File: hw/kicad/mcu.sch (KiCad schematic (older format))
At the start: 36 parts

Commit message: Started working on power supplies
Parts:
- removed C?: 100n, symbol C
- removed C?: 22u, symbol C
- removed C?: 10u, symbol C
- removed U?: AZ1117CR-3.3, TO_SOT_Packages_SMD:SOT89-3_Housing, symbol AZ1117CR-3.3
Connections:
- net I_SENS_A: now also U?.8 (PC0/ADC123_IN10); no longer U?.26 (PB0/ADC12_IN8)
- net I_SENS_B: now also U?.9 (PC1/ADC123_IN11); no longer U?.27 (PB1/ADC12_IN9)
- net I_SENS_C: now also U?.10 (PC2/ADC123_IN12)
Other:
- note removed: "DRV8301: SPI1 (AF5)"
- note removed: "ESR < 20R"
- moved on the sheet: C?, P?, R?

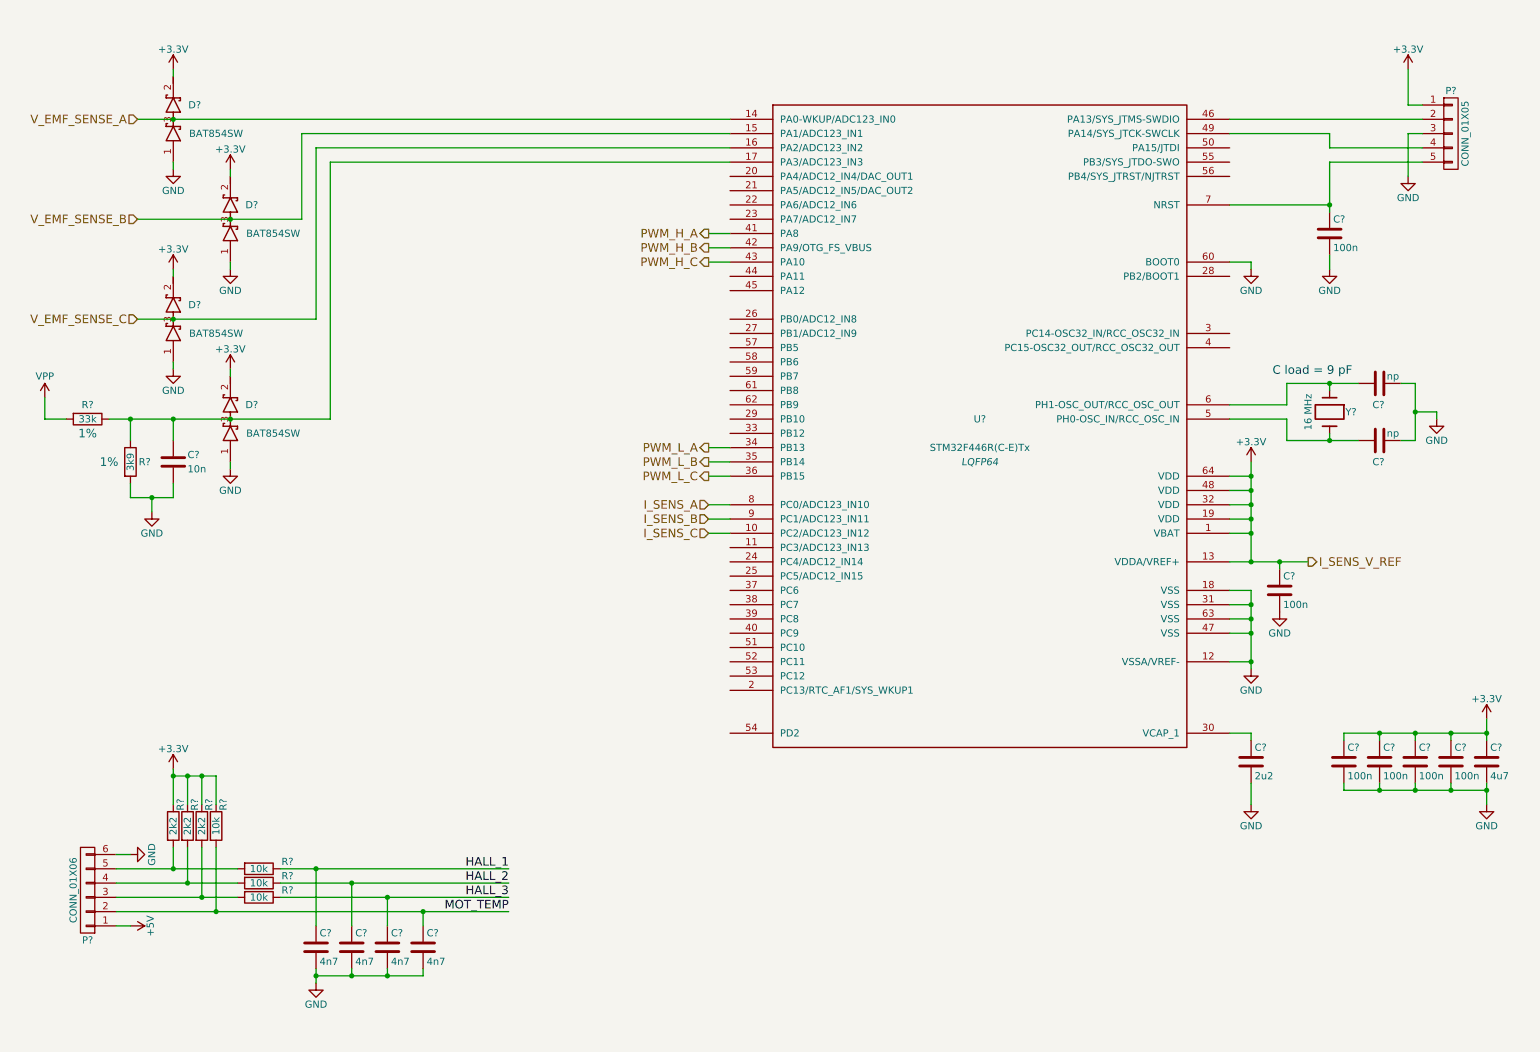
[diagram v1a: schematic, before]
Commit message: Gate power supply enabling and board temp sensor
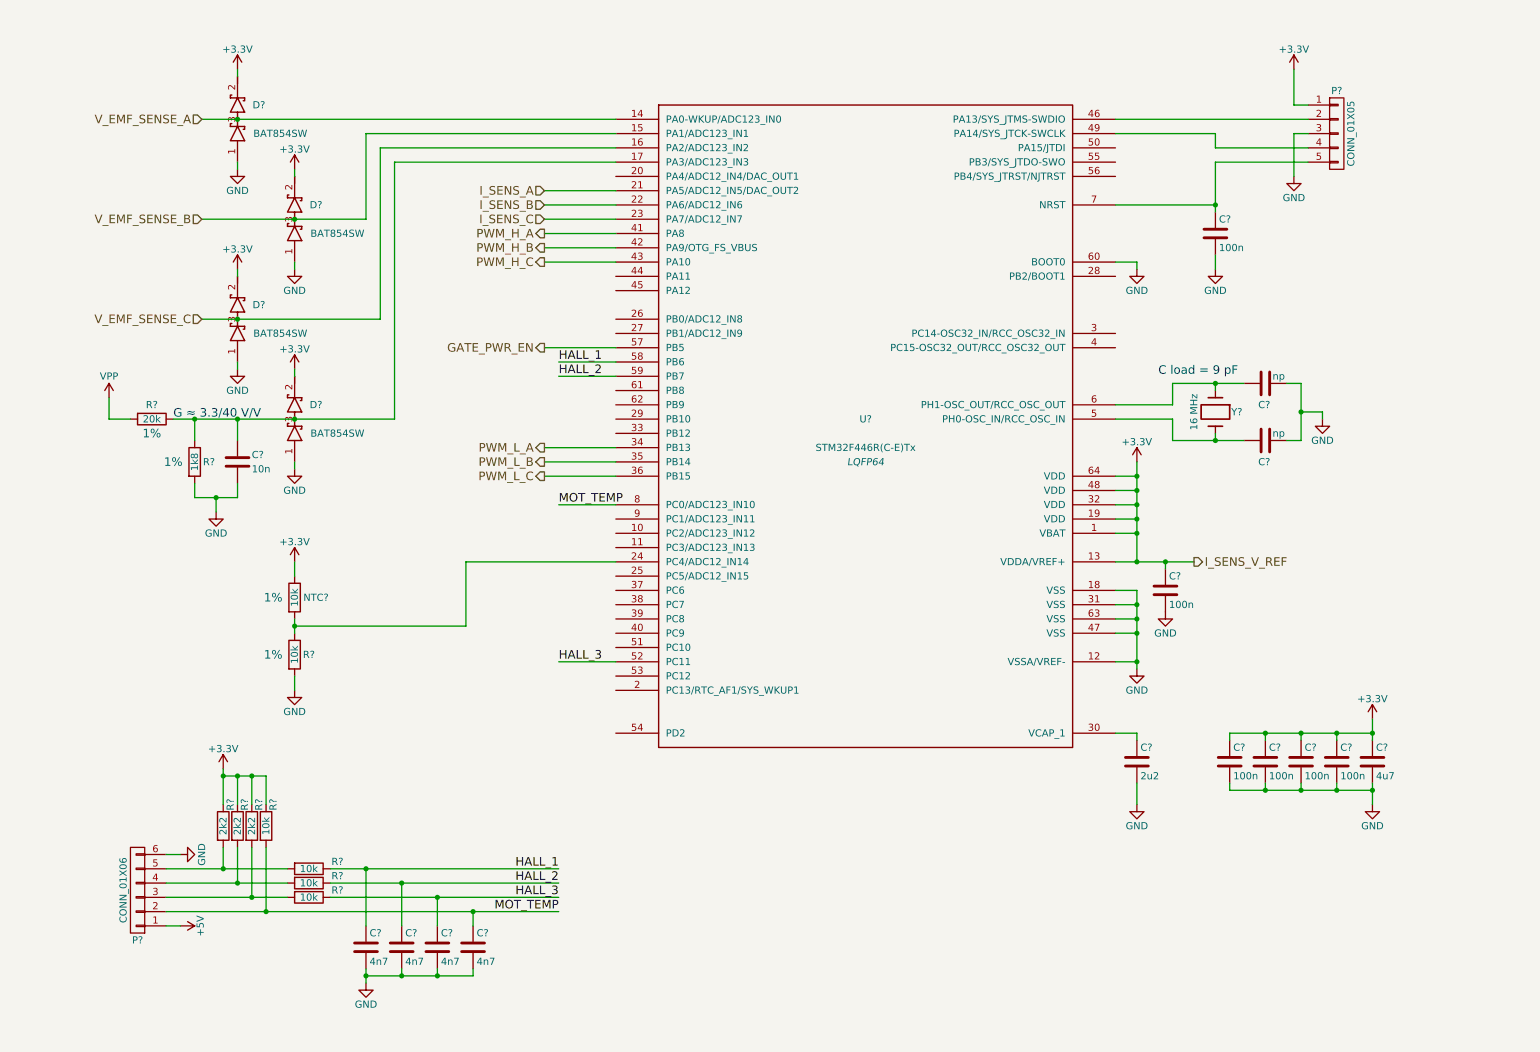
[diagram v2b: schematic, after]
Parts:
- added NTC?: 10k, Resistors_SMD:R_0603, symbol R
- added R?: 10k, symbol R
- R?: value 33k -> 20k
- R?: value 3k9 -> 1k8
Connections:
- net +3V3: now also NTC?.1
- net GND: now also R?.2
- net HALL_1: now also U?.58 (PB6)
- net HALL_2: now also U?.59 (PB7)
- net HALL_3: now also U?.52 (PC11)
- net I_SENS_A: now also U?.21 (PA5/ADC12_IN5/DAC_OUT2); no longer U?.8 (PC0/ADC123_IN10)
- net I_SENS_B: now also U?.22 (PA6/ADC12_IN6); no longer U?.9 (PC1/ADC123_IN11)
- net I_SENS_C: now also U?.23 (PA7/ADC12_IN7); no longer U?.10 (PC2/ADC123_IN12)
- net MOT_TEMP: now also U?.8 (PC0/ADC123_IN10)
- net at U?.24 (PC4/ADC12_IN14): now also NTC?.2, R?.1
- net GATE_PWR_EN: now reaches U?.57 (PB5)
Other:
- note added: "G ≈ 3.3/40 V/V"
- moved on the sheet: C?, D?, P?, R?, U?, Y?

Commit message: TVS across bat connection
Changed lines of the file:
@@
 LIBS:xilinx
 LIBS:Zilog
-LIBS:drv8301
 LIBS:wslp2726
 LIBS:test
@@
 	9000 6000 9000 5950
 Wire Wire Line
-	9000 6000 9250 6000
-Wire Wire Line
-	9250 6000 9500 6000
-Wire Wire Line
-	9500 6000 9750 6000
-Wire Wire Line
-	9750 6000 10000 6000
+	9000 6000 10000 6000
 Wire Wire Line
 	9000 5600 9000 5650
 Wire Wire Line
-	9000 5600 9250 5600
-Wire Wire Line
-	9250 5600 9500 5600
-Wire Wire Line
-	9500 5600 9750 5600
-Wire Wire Line
-	9750 5600 10000 5600
+	9000 5600 10000 5600
 Connection ~ 8350 4700
 Wire Wire Line
@@
 Connection ~ 8350 4900
 Wire Wire Line
-	8350 4600 8350 4700
-Wire Wire Line
-	8350 4700 8350 4800
-Wire Wire Line
-	8350 4800 8350 4900
-Wire Wire Line
-	8350 4900 8350 5100
-Wire Wire Line
-	8350 5100 8350 5150
+	8350 4600 8350 5150
 Wire Wire Line
 	8200 4600 8350 4600
@@
 	8350 4200 8200 4200
 Wire Wire Line
-	8350 3700 8350 3800
-Wire Wire Line
-	8350 3800 8350 3900
-Wire Wire Line
-	8350 3900 8350 4000
-Wire Wire Line
-	8350 4000 8350 4100
-Wire Wire Line
-	8350 4100 8350 4200
-Wire Wire Line
-	8350 4200 8350 4400
+	8350 3700 8350 4400
 Wire Wire Line
 	8200 3800 8350 3800
@@
 	9250 5950 9250 6000
 Wire Wire Line
-	10000 5950 10000 6000
-Wire Wire Line
-	10000 6000 10000 6100
-Wire Wire Line
-	10000 5500 10000 5600
-Wire Wire Line
-	10000 5600 10000 5650
+	10000 5950 10000 6100
+Wire Wire Line
+	10000 5500 10000 5650
 Wire Wire Line
 	8350 5600 8200 5600
@@
 	8350 4900 8200 4900
 Wire Wire Line
-	8200 4400 8350 4400
-Wire Wire Line
-	8350 4400 8550 4400
-Wire Wire Line
-	8550 4400 8750 4400
+	8200 4400 8750 4400
 Connection ~ 8350 4200
 Wire Wire Line
@@
 	9450 1400 9550 1400
 Wire Wire Line
-	8900 1600 8900 1900
-Wire Wire Line
-	8900 1900 8900 1950
+	8900 1600 8900 1950
 Connection ~ 8900 1900
 Wire Wire Line
@@
 	8600 3300 8600 3150
 Wire Wire Line
-	8600 3150 8900 3150
-Wire Wire Line
-	8900 3150 9100 3150
+	8600 3150 9100 3150
 Wire Wire Line
 	8900 3150 8900 3200
@@
 	8900 3500 8900 3550
 Wire Wire Line
-	8600 3550 8900 3550
-Wire Wire Line
-	8900 3550 9100 3550
+	8600 3550 9100 3550
 Wire Wire Line
 	8600 3550 8600 3400
@@
 	9400 3150 9500 3150
 Wire Wire Line
-	9500 3150 9500 3350
-Wire Wire Line
-	9500 3350 9500 3550
+	9500 3150 9500 3550
 Wire Wire Line
 	9500 3350 9650 3350
@@
 	2050 3050 2050 3000
 Wire Wire Line
-	1800 2700 2050 2700
-Wire Wire Line
-	2050 2700 3050 2700
+	1800 2700 3050 2700
 Wire Wire Line
 	2050 2400 2050 2350
@@
 Connection ~ 2450 2000
 Wire Wire Line
-	1800 1300 2050 1300
-Wire Wire Line
-	2050 1300 4700 1300
+	1800 1300 4700 1300
 Connection ~ 2050 1300
 Wire Wire Line
@@
 	4700 1400 2950 1400
 Wire Wire Line
-	2950 1400 2950 2000
-Wire Wire Line
-	2950 2000 2450 2000
-Wire Wire Line
-	2450 2000 1800 2000
+	2950 2000 2950 1400
+Wire Wire Line
+	1800 2000 2950 2000
 Wire Wire Line
 	3050 2700 3050 1500
@@
 	1550 6450 1650 6450
 Wire Wire Line
-	1550 6550 1950 6550
-Wire Wire Line
-	1950 6550 2400 6550
+	1550 6550 2400 6550
 Wire Wire Line
 	1950 6550 1950 6400
 Wire Wire Line
-	1550 6650 2050 6650
-Wire Wire Line
-	2050 6650 2400 6650
+	1550 6650 2400 6650
 Wire Wire Line
 	2050 6650 2050 6400
 Wire Wire Line
-	1550 6750 2150 6750
-Wire Wire Line
-	2150 6750 2400 6750
+	1550 6750 2400 6750
 Wire Wire Line
 	2150 6750 2150 6400
 Wire Wire Line
-	1550 6850 2250 6850
-Wire Wire Line
-	2250 6850 3700 6850
-Wire Wire Line
-	3700 6850 4300 6850
+	1550 6850 4300 6850
 Wire Wire Line
 	2250 6850 2250 6400
@@
 Connection ~ 2150 6750
 Wire Wire Line
-	2700 6550 2950 6550
-Wire Wire Line
-	2950 6550 4300 6550
+	2700 6550 4300 6550
 Wire Wire Line
 	2950 6550 2950 6950
 Wire Wire Line
-	2700 6650 3200 6650
-Wire Wire Line
-	3200 6650 4300 6650
+	2700 6650 4300 6650
 Wire Wire Line
 	3200 6650 3200 6950
 Wire Wire Line
-	2700 6750 3450 6750
-Wire Wire Line
-	3450 6750 4300 6750
+	2700 6750 4300 6750
 Wire Wire Line
 	3450 6750 3450 6950
 Wire Wire Line
-	2950 7250 2950 7300
-Wire Wire Line
-	2950 7300 2950 7350
-Wire Wire Line
-	2950 7300 3200 7300
-Wire Wire Line
-	3200 7300 3450 7300
-Wire Wire Line
-	3450 7300 3700 7300
+	2950 7250 2950 7350
+Wire Wire Line
+	2950 7300 3700 7300
 Wire Wire Line
 	3200 7300 3200 7250
@@
 $EndComp
 Wire Wire Line
-	1950 5850 1950 5900
-Wire Wire Line
-	1950 5900 1950 6100
-Wire Wire Line
-	1950 5900 2050 5900
-Wire Wire Line
-	2050 5900 2150 5900
-Wire Wire Line
-	2150 5900 2250 5900
+	1950 5850 1950 6100
+Wire Wire Line
+	1950 5900 2250 5900
 Wire Wire Line
 	2250 5900 2250 6100
@@
 	1900 3950 1900 4050
 Wire Wire Line
-	1750 3950 1900 3950
-Wire Wire Line
-	1900 3950 2050 3950
+	1750 3950 2050 3950
 Wire Wire Line
 	1750 3850 1750 3950
@@
 	2050 3400 2050 3550
 Wire Wire Line
-	1600 3400 1750 3400
-Wire Wire Line
-	1750 3400 2050 3400
-Wire Wire Line
-	2050 3400 2450 3400
-Wire Wire Line
-	2450 3400 3150 3400
+	1600 3400 3150 3400
 Connection ~ 2050 3400
 Wire Wire Line
@@
 	2450 5300 2450 5200
 Wire Wire Line
-	2450 4900 2450 4850
-Wire Wire Line
-	2450 4850 2450 4800
+	2450 4800 2450 4900
 Wire Wire Line
 	4700 4400 3650 4400

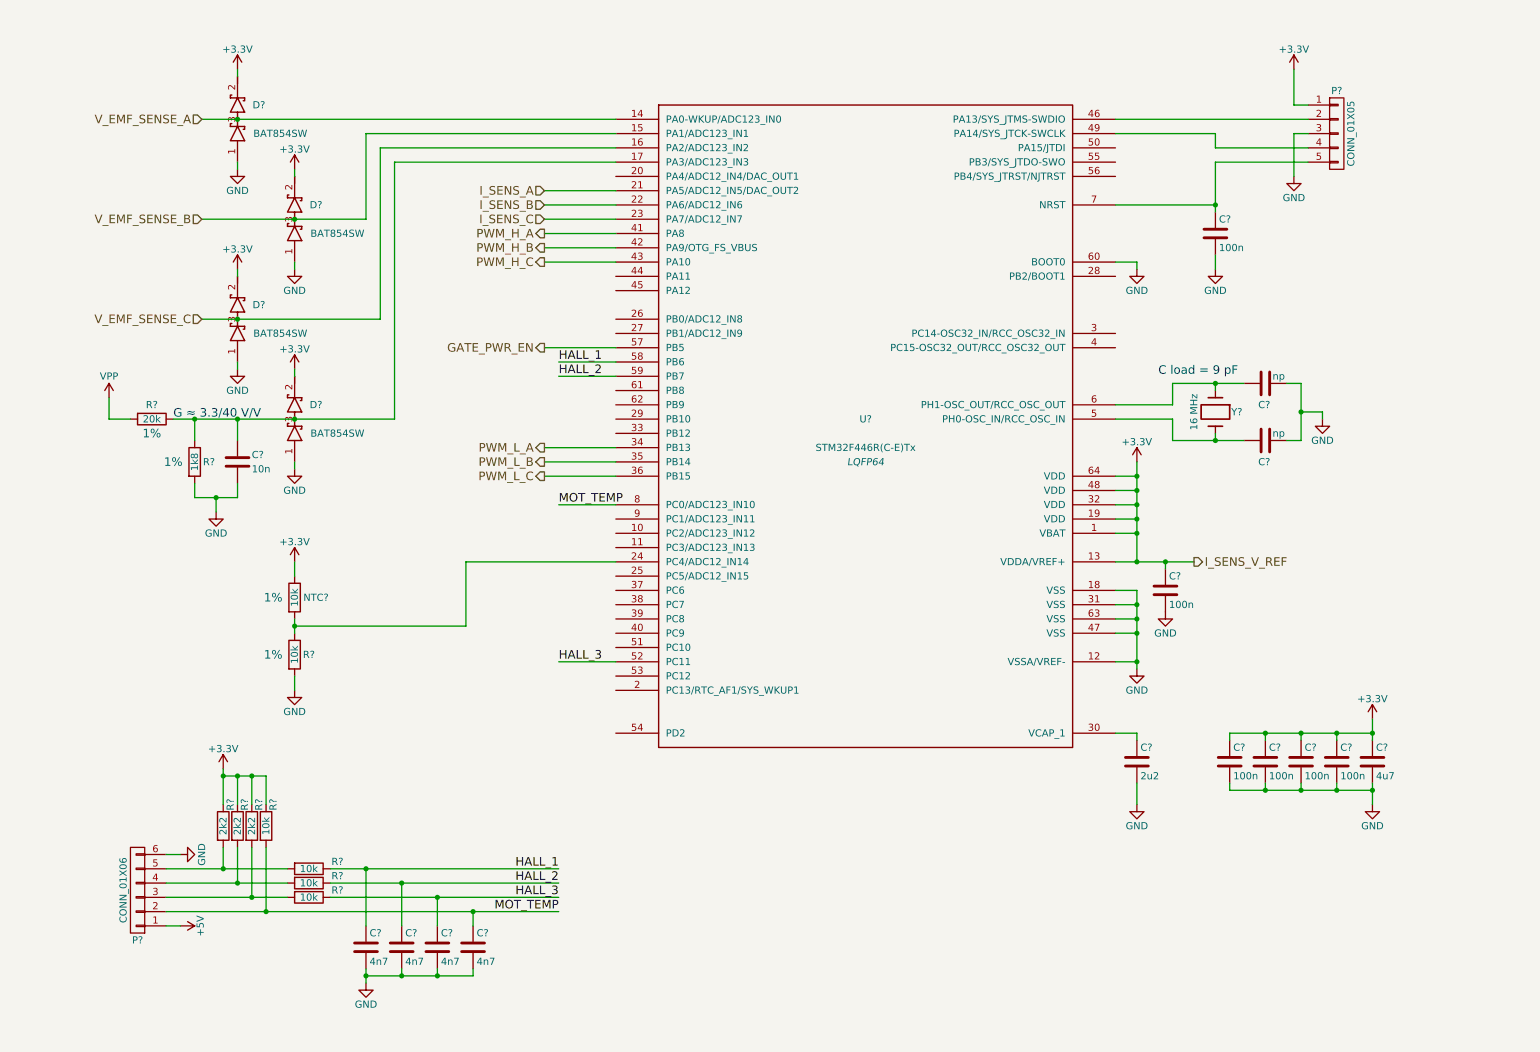
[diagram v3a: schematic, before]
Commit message: Bat pads and leds
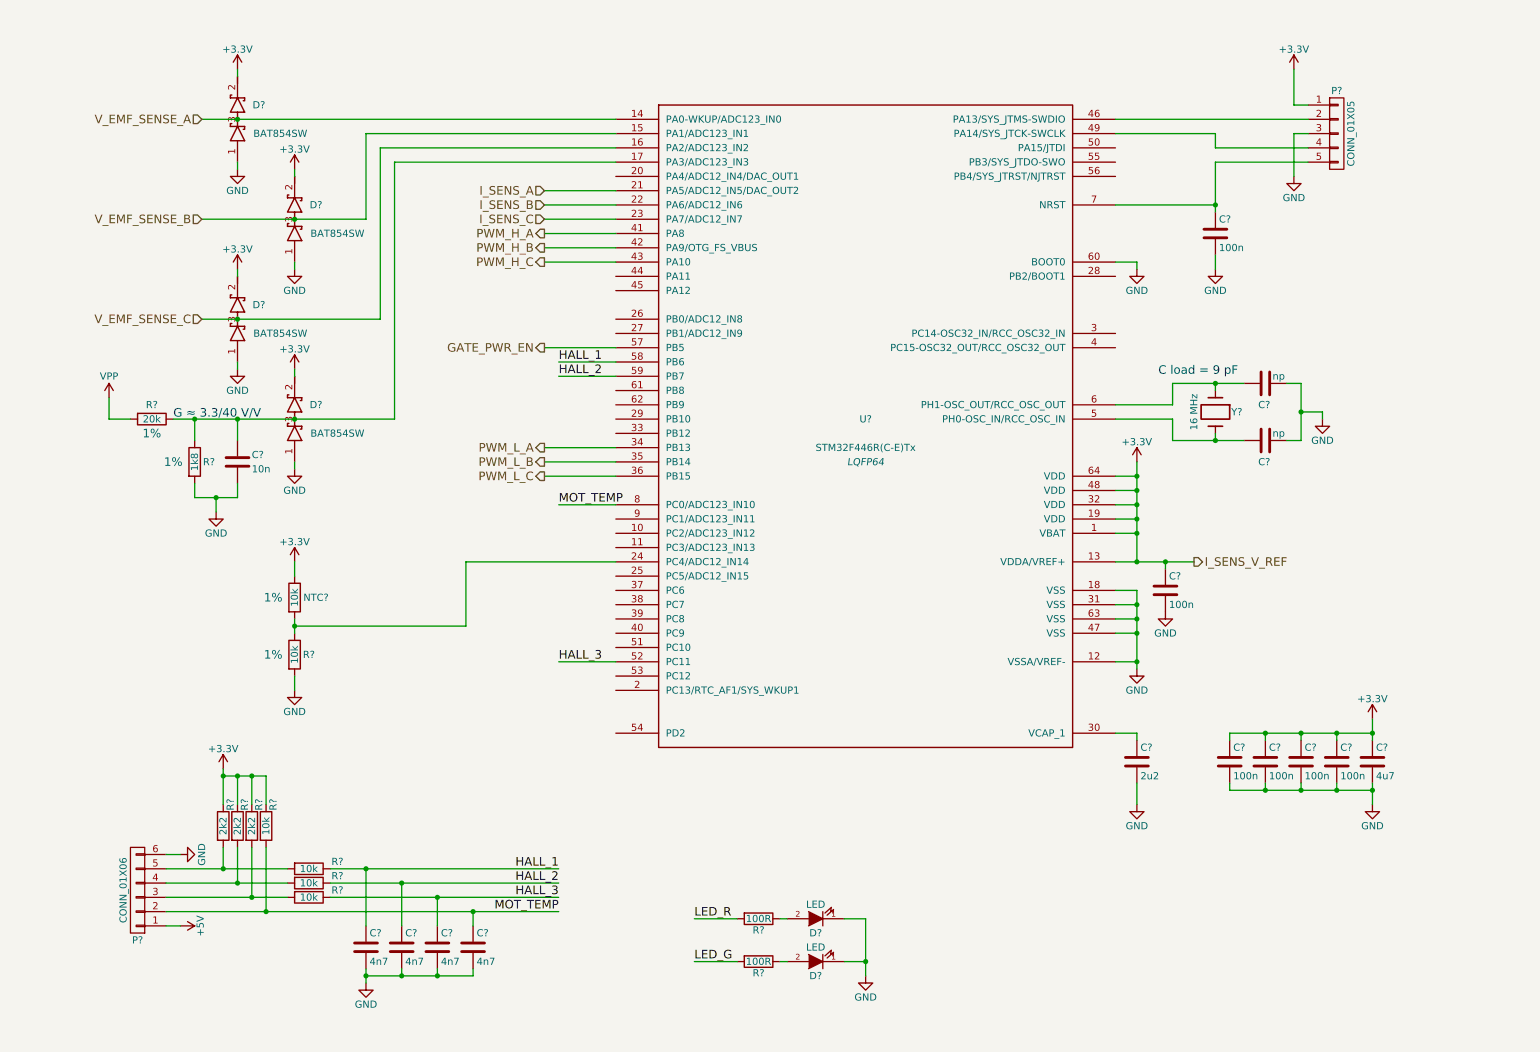
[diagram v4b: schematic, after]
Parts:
- added D? (x2): LED, symbol LED
- added R? (x2): 100R, symbol R
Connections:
- net GND: now also D?.1 (K), D?.1 (K)
- new net: D?.2 (A), R?.1 (x2)
- new net LED_G: R?.2
- new net LED_R: R?.2
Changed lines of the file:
@@
 	4700 1400 2950 1400
 Wire Wire Line
-	2950 2000 2950 1400
-Wire Wire Line
-	1800 2000 2950 2000
+	2950 1400 2950 2000
+Wire Wire Line
+	2950 2000 1800 2000
 Wire Wire Line
 	3050 2700 3050 1500
@@
 	3650 4850 3650 4400
 Connection ~ 2450 4850
+$Comp
+L LED D?
+U 1 1 58362F24
+P 6100 7200
+F 0 "D?" H 6100 7300 50  0000 C CNN
+F 1 "LED" H 6100 7100 50  0000 C CNN
+F 2 "" H 6100 7200 60  0000 C CNN
+F 3 "" H 6100 7200 60  0000 C CNN
+	1    6100 7200
+	-1   0    0    1
+$EndComp
+$Comp
+L LED D?
+U 1 1 583633B5
+P 6100 6900
+F 0 "D?" H 6100 7000 50  0000 C CNN
+F 1 "LED" H 6100 6800 50  0000 C CNN
+F 2 "" H 6100 6900 60  0000 C CNN
+F 3 "" H 6100 6900 60  0000 C CNN
+	1    6100 6900
+	-1   0    0    1
+$EndComp
+Wire Wire Line
+	6300 6900 6450 6900
+Wire Wire Line
+	6450 6900 6450 7300
+Wire Wire Line
+	6300 7200 6450 7200
+Connection ~ 6450 7200
+$Comp
+L GND #PWR?
+U 1 1 58363604
+P 6450 7300
+F 0 "#PWR?" H 6450 7050 50  0001 C CNN
+F 1 "GND" H 6450 7150 50  0000 C CNN
+F 2 "" H 6450 7300 60  0000 C CNN
+F 3 "" H 6450 7300 60  0000 C CNN
+	1    6450 7300
+	1    0    0    -1
+$EndComp
+$Comp
+L R R?
+U 1 1 58363C15
+P 5700 6900
+F 0 "R?" V 5780 6900 50  0000 C CNN
+F 1 "100R" V 5700 6900 50  0000 C CNN
+F 2 "" V 5630 6900 30  0000 C CNN
+F 3 "" H 5700 6900 30  0000 C CNN
+	1    5700 6900
+	0    1    1    0
+$EndComp
+$Comp
+L R R?
+U 1 1 58363D14
+P 5700 7200
+F 0 "R?" V 5780 7200 50  0000 C CNN
+F 1 "100R" V 5700 7200 50  0000 C CNN
+F 2 "" V 5630 7200 30  0000 C CNN
+F 3 "" H 5700 7200 30  0000 C CNN
+	1    5700 7200
+	0    1    1    0
+$EndComp
+Wire Wire Line
+	5850 7200 5900 7200
+Wire Wire Line
+	5850 6900 5900 6900
+Text Label 5250 6900 0    60   ~ 0
+LED_R
+Wire Wire Line
+	5250 6900 5550 6900
+Wire Wire Line
+	5550 7200 5250 7200
+Text Label 5250 7200 0    60   ~ 0
+LED_G
 $EndSCHEMATC
